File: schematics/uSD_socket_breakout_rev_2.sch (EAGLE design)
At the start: 4 parts

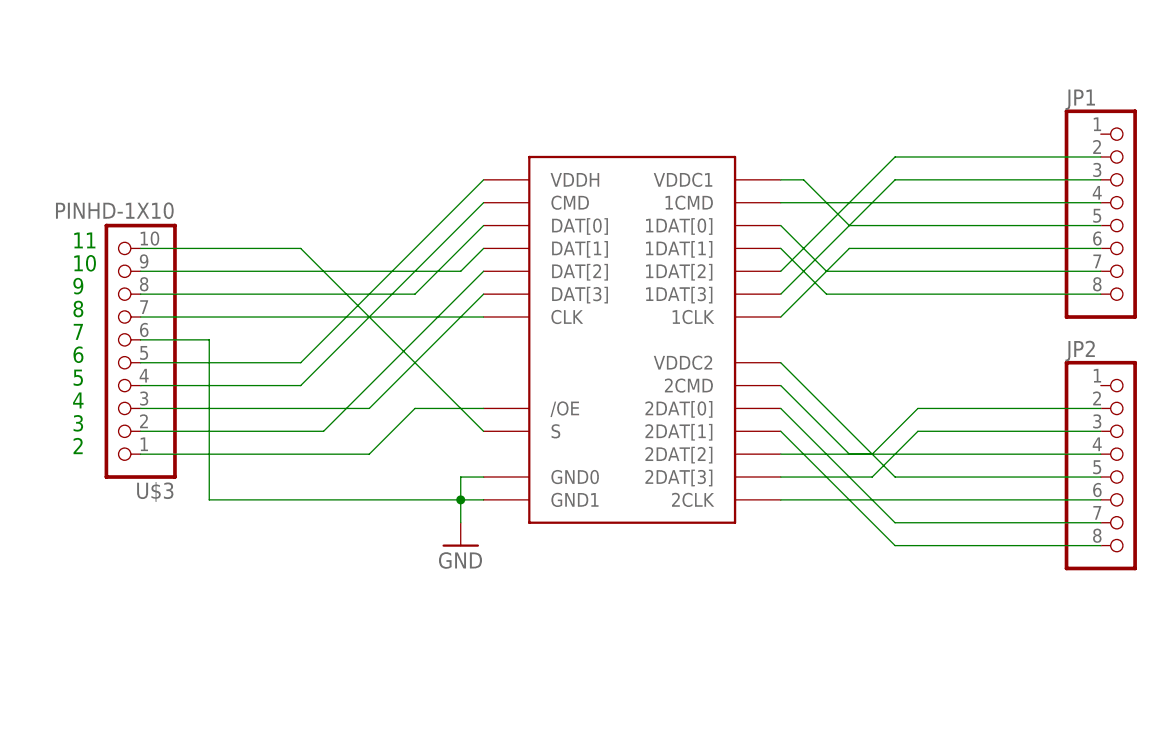
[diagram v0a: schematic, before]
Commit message: Breakout boards for MUX and uSD socket, updated mux+uSD schematic
Built individual breakout boards for MUX chip and uSD socket.
Discovered errors in MUX and uSD integrated board and updated
schematic--ripped up wrong connections in .brd file but did not bother
rerouting traces since this board will most likely not be fabbed again.
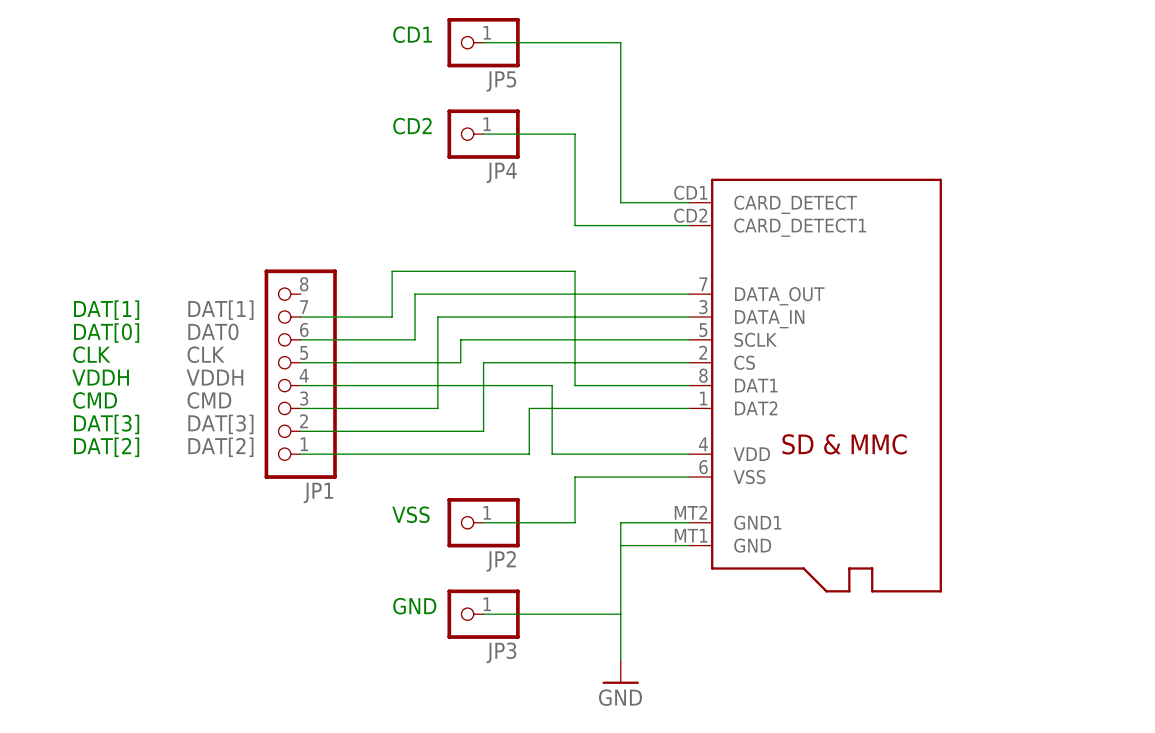
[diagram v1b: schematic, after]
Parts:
- removed U$3: PINHD-1X10, adafruit:PINHD-1X10
- added JP3, JP4, JP5: (no value), adafruit:PINHD-1X1CB
- JP2: device adafruit:PINHD-1X8CLEANBIG -> adafruit:PINHD-1X1CB
- U$1: value (none) -> MICROSD; device FSSD06_MLP24a:FSSD06 -> adafruit:MICROSD
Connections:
- removed net /OE: U$1./OE, U$3.1
- removed net 1CLK: JP1.6, U$1.1CLK
- removed net 1CMD: JP1.4, U$1.1CMD
- removed net 1DAT[0]: JP1.7, U$1.1DAT[0]
- removed net 1DAT[1]: JP1.8, U$1.1DAT[1]
- removed net 1DAT[2]: JP1.2, U$1.1DAT[2]
- removed net 1DAT[3]: JP1.3, U$1.1DAT[3]
- removed net 2CLK: JP2.6, U$1.2CLK
- removed net 2CMD: JP2.4, U$1.2CMD
- removed net 2DAT3: JP2.3, U$1.2DAT[3]
- removed net 2DAT[0]: JP2.7, U$1.2DAT[0]
- removed net 2DAT[1]: JP2.8, U$1.2DAT[1]
- removed net 2DAT[2]: JP2.2, U$1.2DAT[2]
- removed net DAT[0]: U$1.DAT[0], U$3.8
- removed net S: U$1.S, U$3.10
- removed net VDDC1: JP1.5, U$1.VDDC1
- removed net VDDC2: JP2.5, U$1.VDDC2
- new net DAT0: JP1.6, U$1.DATA_OUT
- new net N$3: JP5.1, U$1.CARD_DETECT
- new net N$4: JP4.1, U$1.CARD_DETECT1
- new net VSS: JP2.1, U$1.VSS
- net CLK: now also JP1.5, U$1.SCLK; no longer U$1.CLK, U$3.7
- net CMD: now also JP1.3, U$1.DATA_IN; no longer U$1.CMD, U$3.4
- net DAT[1]: now also JP1.7, U$1.DAT1; no longer U$1.DAT[1], U$3.9
- net DAT[2]: now also JP1.1, U$1.DAT2; no longer U$1.DAT[2], U$3.2
- net DAT[3]: now also JP1.2, U$1.CS; no longer U$1.DAT[3], U$3.3
- net GND: now also JP3.1, U$1.GND; no longer U$1.GND0, U$3.6
- net VDDH: now also JP1.4, U$1.VDD; no longer U$1.VDDH, U$3.5
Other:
- note added: "CD1"
- note added: "CD2"
- note added: "CLK"
- note added: "CMD"
- note added: "DAT[0]"
- note added: "DAT[1]"
- note added: "DAT[2]"
- note added: "DAT[3]"
- note added: "GND"
- note added: "VDDH"
- note added: "VSS"
- note removed: "10"
- note removed: "11"
- note removed: "2"
- note removed: "3"
- note removed: "4"
- note removed: "5"
- note removed: "6"
- note removed: "7"
- note removed: "8"
- note removed: "9"
- moved on the sheet: JP1
